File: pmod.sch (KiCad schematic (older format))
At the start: 13 parts, among them J6 PMOD, U10 AP7381-33SA, U11 TXS0108EPW

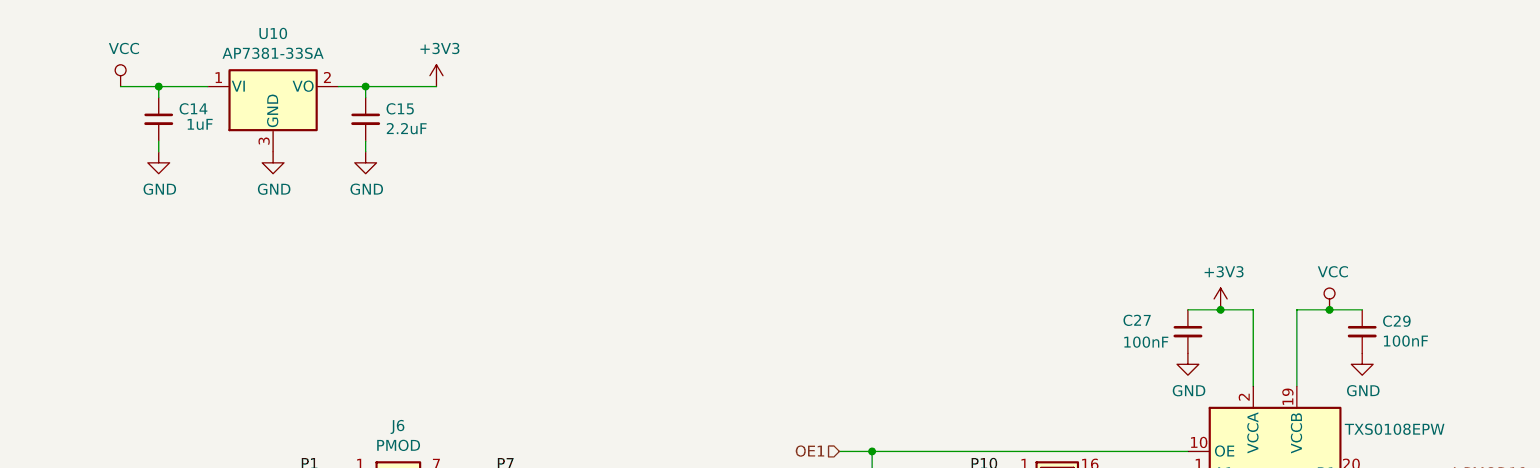
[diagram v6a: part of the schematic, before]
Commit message: replaced VCC with 5V, fixed ROM footprint
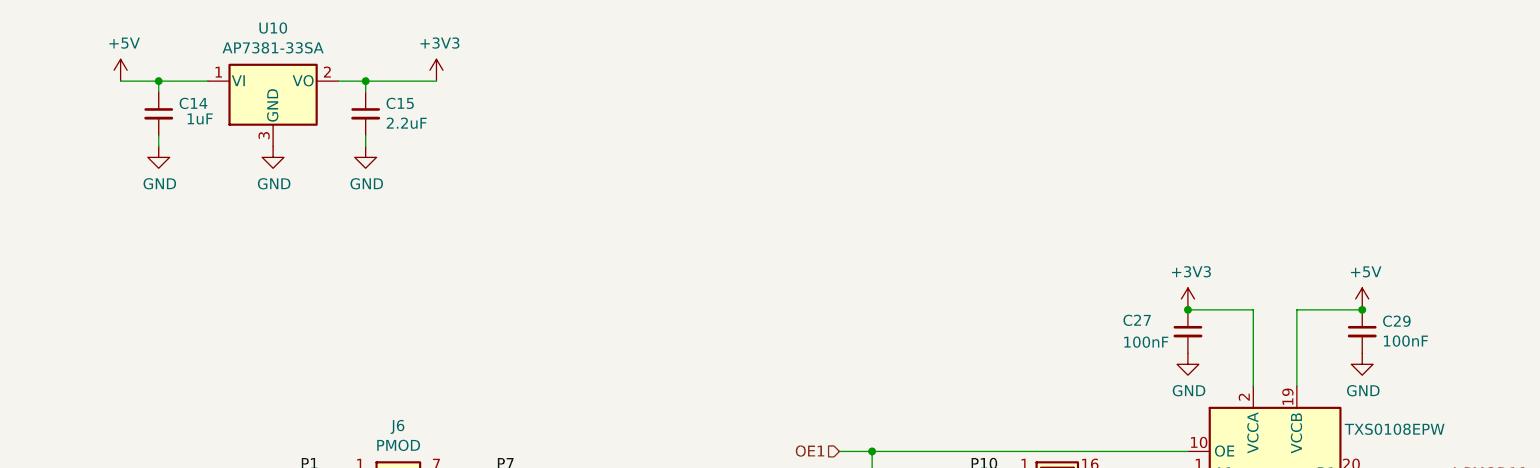
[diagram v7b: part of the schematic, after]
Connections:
- net labels added: +5V
- net labels removed: VCC
- wire segments 68 -> 66
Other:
- moved on the sheet: C14, C15, U10
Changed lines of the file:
@@
 	1925 3800 1925 3400
-$Comp
-L power:VCC #PWR?
-U 1 1 5DC93B40
-P 1850 1625
-AR Path="/5D70CA34/5DC93B40" Ref="#PWR?"  Part="1"
-AR Path="/5D70CA34/5DC790D1/5DC93B40" Ref="#PWR033"  Part="1"
-F 0 "#PWR033" H 1850 1475 50  0001 C CNN
-F 1 "VCC" H 1867 1798 50  0000 C CNN
-F 2 "" H 1850 1625 50  0001 C CNN
-F 3 "" H 1850 1625 50  0001 C CNN
-	1    1850 1625
-	1    0    0    -1
-$EndComp
 $Comp
 L power:+3V3 #PWR?
 U 1 1 5DC93B46
-P 3300 1625
+P 3300 1600
 AR Path="/5D70CA34/5DC93B46" Ref="#PWR?"  Part="1"
 AR Path="/5D70CA34/5DC790D1/5DC93B46" Ref="#PWR077"  Part="1"
-F 0 "#PWR077" H 3300 1475 50  0001 C CNN
-F 1 "+3V3" H 3315 1798 50  0000 C CNN
-F 2 "" H 3300 1625 50  0001 C CNN
-F 3 "" H 3300 1625 50  0001 C CNN
-	1    3300 1625
-	1    0    0    -1
-$EndComp
-Wire Wire Line
-	2025 1625 1850 1625
-Connection ~ 2025 1625
-Wire Wire Line
-	2025 1675 2025 1625
-Wire Wire Line
-	2975 1625 3300 1625
-Connection ~ 2975 1625
-Wire Wire Line
-	2975 1675 2975 1625
-Wire Wire Line
-	2850 1625 2975 1625
-Wire Wire Line
-	2250 1625 2025 1625
+F 0 "#PWR077" H 3300 1450 50  0001 C CNN
+F 1 "+3V3" H 3315 1773 50  0000 C CNN
+F 2 "" H 3300 1600 50  0001 C CNN
+F 3 "" H 3300 1600 50  0001 C CNN
+	1    3300 1600
+	1    0    0    -1
+$EndComp
+Wire Wire Line
+	2025 1600 1850 1600
+Connection ~ 2025 1600
+Wire Wire Line
+	2025 1650 2025 1600
+Wire Wire Line
+	2975 1600 3300 1600
+Connection ~ 2975 1600
+Wire Wire Line
+	2975 1650 2975 1600
+Wire Wire Line
+	2850 1600 2975 1600
+Wire Wire Line
+	2250 1600 2025 1600
 $Comp
 L power:GND #PWR?
 U 1 1 5DC93B54
-P 2550 1925
+P 2550 1900
 AR Path="/5D70CA34/5DC93B54" Ref="#PWR?"  Part="1"
 AR Path="/5D70CA34/5DC790D1/5DC93B54" Ref="#PWR036"  Part="1"
-F 0 "#PWR036" H 2550 1675 50  0001 C CNN
-F 1 "GND" H 2555 1752 50  0000 C CNN
-F 2 "" H 2550 1925 50  0001 C CNN
-F 3 "" H 2550 1925 50  0001 C CNN
-	1    2550 1925
+F 0 "#PWR036" H 2550 1650 50  0001 C CNN
+F 1 "GND" H 2555 1727 50  0000 C CNN
+F 2 "" H 2550 1900 50  0001 C CNN
+F 3 "" H 2550 1900 50  0001 C CNN
+	1    2550 1900
 	1    0    0    -1
 $EndComp
@@
 L power:GND #PWR?
 U 1 1 5DC93B5A
-P 2025 1925
+P 2025 1900
 AR Path="/5D70CA34/5DC93B5A" Ref="#PWR?"  Part="1"
 AR Path="/5D70CA34/5DC790D1/5DC93B5A" Ref="#PWR034"  Part="1"
-F 0 "#PWR034" H 2025 1675 50  0001 C CNN
-F 1 "GND" H 2030 1752 50  0000 C CNN
-F 2 "" H 2025 1925 50  0001 C CNN
-F 3 "" H 2025 1925 50  0001 C CNN
-	1    2025 1925
-	1    0    0    -1
-$EndComp
-Wire Wire Line
-	2025 1875 2025 1925
+F 0 "#PWR034" H 2025 1650 50  0001 C CNN
+F 1 "GND" H 2030 1727 50  0000 C CNN
+F 2 "" H 2025 1900 50  0001 C CNN
+F 3 "" H 2025 1900 50  0001 C CNN
+	1    2025 1900
+	1    0    0    -1
+$EndComp
+Wire Wire Line
+	2025 1850 2025 1900
 $Comp
 L Device:C_Small C?
 U 1 1 5DC93B61
-P 2025 1775
+P 2025 1750
 AR Path="/5D70CA34/5DC93B61" Ref="C?"  Part="1"
 AR Path="/5D70CA34/5DC790D1/5DC93B61" Ref="C14"  Part="1"
-F 0 "C14" H 2117 1821 50  0000 L CNN
-F 1 "1uF" H 2150 1750 50  0000 L CNN
-F 2 "Capacitor_SMD:C_0603_1608Metric_Pad1.05x0.95mm_HandSolder" H 2025 1775 50  0001 C CNN
-F 3 "~" H 2025 1775 50  0001 C CNN
-	1    2025 1775
+F 0 "C14" H 2117 1796 50  0000 L CNN
+F 1 "1uF" H 2150 1725 50  0000 L CNN
+F 2 "Capacitor_SMD:C_0603_1608Metric_Pad1.05x0.95mm_HandSolder" H 2025 1750 50  0001 C CNN
+F 3 "~" H 2025 1750 50  0001 C CNN
+	1    2025 1750
 	1    0    0    -1
 $EndComp
@@
 L power:GND #PWR?
 U 1 1 5DC93B67
-P 2975 1925
+P 2975 1900
 AR Path="/5D70CA34/5DC93B67" Ref="#PWR?"  Part="1"
 AR Path="/5D70CA34/5DC790D1/5DC93B67" Ref="#PWR038"  Part="1"
-F 0 "#PWR038" H 2975 1675 50  0001 C CNN
-F 1 "GND" H 2980 1752 50  0000 C CNN
-F 2 "" H 2975 1925 50  0001 C CNN
-F 3 "" H 2975 1925 50  0001 C CNN
-	1    2975 1925
-	1    0    0    -1
-$EndComp
-Wire Wire Line
-	2975 1875 2975 1925
+F 0 "#PWR038" H 2975 1650 50  0001 C CNN
+F 1 "GND" H 2980 1727 50  0000 C CNN
+F 2 "" H 2975 1900 50  0001 C CNN
+F 3 "" H 2975 1900 50  0001 C CNN
+	1    2975 1900
+	1    0    0    -1
+$EndComp
+Wire Wire Line
+	2975 1850 2975 1900
 $Comp
 L Device:C_Small C?
 U 1 1 5DC93B6E
-P 2975 1775
+P 2975 1750
 AR Path="/5D70CA34/5DC93B6E" Ref="C?"  Part="1"
 AR Path="/5D70CA34/5DC790D1/5DC93B6E" Ref="C15"  Part="1"
-F 0 "C15" H 3067 1821 50  0000 L CNN
-F 1 "2.2uF" H 3067 1730 50  0000 L CNN
-F 2 "Capacitor_SMD:C_0603_1608Metric_Pad1.05x0.95mm_HandSolder" H 2975 1775 50  0001 C CNN
-F 3 "~" H 2975 1775 50  0001 C CNN
-	1    2975 1775
+F 0 "C15" H 3067 1796 50  0000 L CNN
+F 1 "2.2uF" H 3067 1705 50  0000 L CNN
+F 2 "Capacitor_SMD:C_0603_1608Metric_Pad1.05x0.95mm_HandSolder" H 2975 1750 50  0001 C CNN
+F 3 "~" H 2975 1750 50  0001 C CNN
+	1    2975 1750
 	1    0    0    -1
 $EndComp
@@
 L THS-80-rescue:AP7381-33SA-Regulator_Linear U?
 U 1 1 5DC93B74
-P 2550 1625
+P 2550 1600
 AR Path="/5D70CA34/5DC93B74" Ref="U?"  Part="1"
 AR Path="/5D70CA34/5DC790D1/5DC93B74" Ref="U10"  Part="1"
 AR Path="/5DC93B74" Ref="U10"  Part="1"
-F 0 "U10" H 2550 1867 50  0000 C CNN
-F 1 "AP7381-33SA" H 2550 1776 50  0000 C CNN
-F 2 "Package_TO_SOT_SMD:SOT-23" H 2550 1850 50  0001 C CIN
-F 3 "https://www.mouser.com/datasheet/2/115/AP7381-1220674.pdf" H 2550 1575 50  0001 C CNN
-	1    2550 1625
+F 0 "U10" H 2550 1842 50  0000 C CNN
+F 1 "AP7381-33SA" H 2550 1751 50  0000 C CNN
+F 2 "Package_TO_SOT_SMD:SOT-23" H 2550 1825 50  0001 C CIN
+F 3 "https://www.mouser.com/datasheet/2/115/AP7381-1220674.pdf" H 2550 1550 50  0001 C CNN
+	1    2550 1600
 	1    0    0    -1
 $EndComp
@@
 $EndComp
 $Comp
-L power:VCC #PWR?
-U 1 1 5DEF913A
-P 7400 2650
-AR Path="/5D70CA34/5DEF913A" Ref="#PWR?"  Part="1"
-AR Path="/5D70CA34/5DC790D1/5DEF913A" Ref="#PWR0103"  Part="1"
-F 0 "#PWR0103" H 7400 2500 50  0001 C CNN
-F 1 "VCC" H 7417 2823 50  0000 C CNN
-F 2 "" H 7400 2650 50  0001 C CNN
-F 3 "" H 7400 2650 50  0001 C CNN
-	1    7400 2650
-	1    0    0    -1
-$EndComp
-$Comp
 L Logic_LevelTranslator:TXS0108EPW U11
 U 1 1 5DF4B0EE
@@
 L power:+3V3 #PWR0105
 U 1 1 5DF9A54A
-P 6900 2650
-F 0 "#PWR0105" H 6900 2500 50  0001 C CNN
-F 1 "+3V3" H 6915 2823 50  0000 C CNN
-F 2 "" H 6900 2650 50  0001 C CNN
-F 3 "" H 6900 2650 50  0001 C CNN
-	1    6900 2650
+P 6750 2650
+F 0 "#PWR0105" H 6750 2500 50  0001 C CNN
+F 1 "+3V3" H 6765 2823 50  0000 C CNN
+F 2 "" H 6750 2650 50  0001 C CNN
+F 3 "" H 6750 2650 50  0001 C CNN
+	1    6750 2650
 	1    0    0    -1
 $EndComp
@@
 	7250 3000 7250 2650
 Wire Wire Line
-	7250 2650 7400 2650
-Connection ~ 7400 2650
-Wire Wire Line
-	7400 2650 7550 2650
-Wire Wire Line
 	7050 3000 7050 2650
-Wire Wire Line
-	7050 2650 6900 2650
-Connection ~ 6900 2650
-Wire Wire Line
-	6900 2650 6750 2650
+$Comp
+L power:+5V #PWR0128
+U 1 1 5EB06066
+P 1850 1600
+F 0 "#PWR0128" H 1850 1450 50  0001 C CNN
+F 1 "+5V" H 1865 1773 50  0000 C CNN
+F 2 "" H 1850 1600 50  0001 C CNN
+F 3 "" H 1850 1600 50  0001 C CNN
+	1    1850 1600
+	1    0    0    -1
+$EndComp
+Wire Wire Line
+	7250 2650 7550 2650
+$Comp
+L power:+5V #PWR0129
+U 1 1 5EB0BA2B
+P 7550 2650
+F 0 "#PWR0129" H 7550 2500 50  0001 C CNN
+F 1 "+5V" H 7565 2823 50  0000 C CNN
+F 2 "" H 7550 2650 50  0001 C CNN
+F 3 "" H 7550 2650 50  0001 C CNN
+	1    7550 2650
+	1    0    0    -1
+$EndComp
+Connection ~ 7550 2650
+Connection ~ 6750 2650
+Wire Wire Line
+	6750 2650 7050 2650
 $EndSCHEMATC

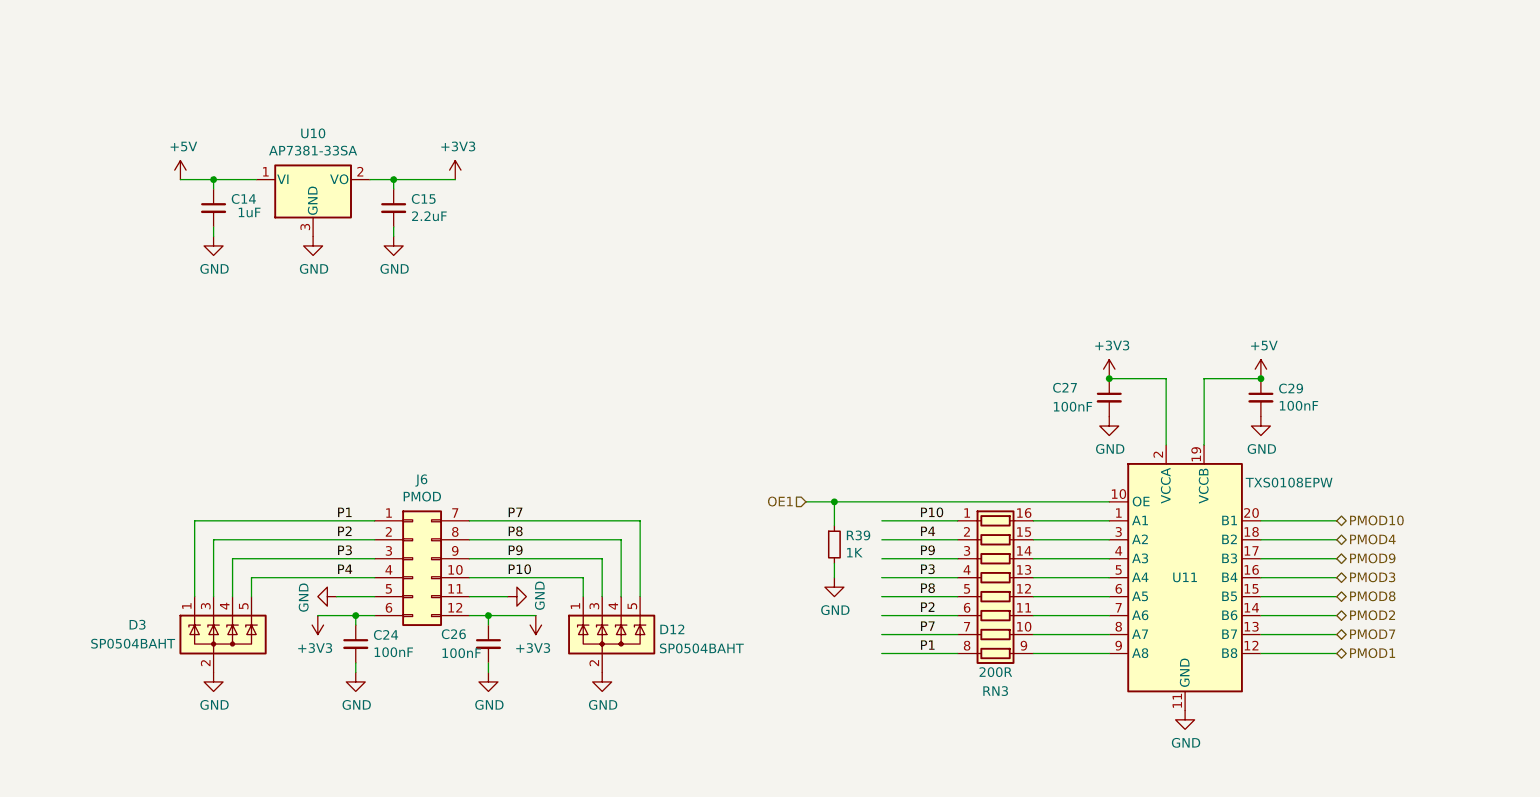
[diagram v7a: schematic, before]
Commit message: layout changes, silkscreen fixes
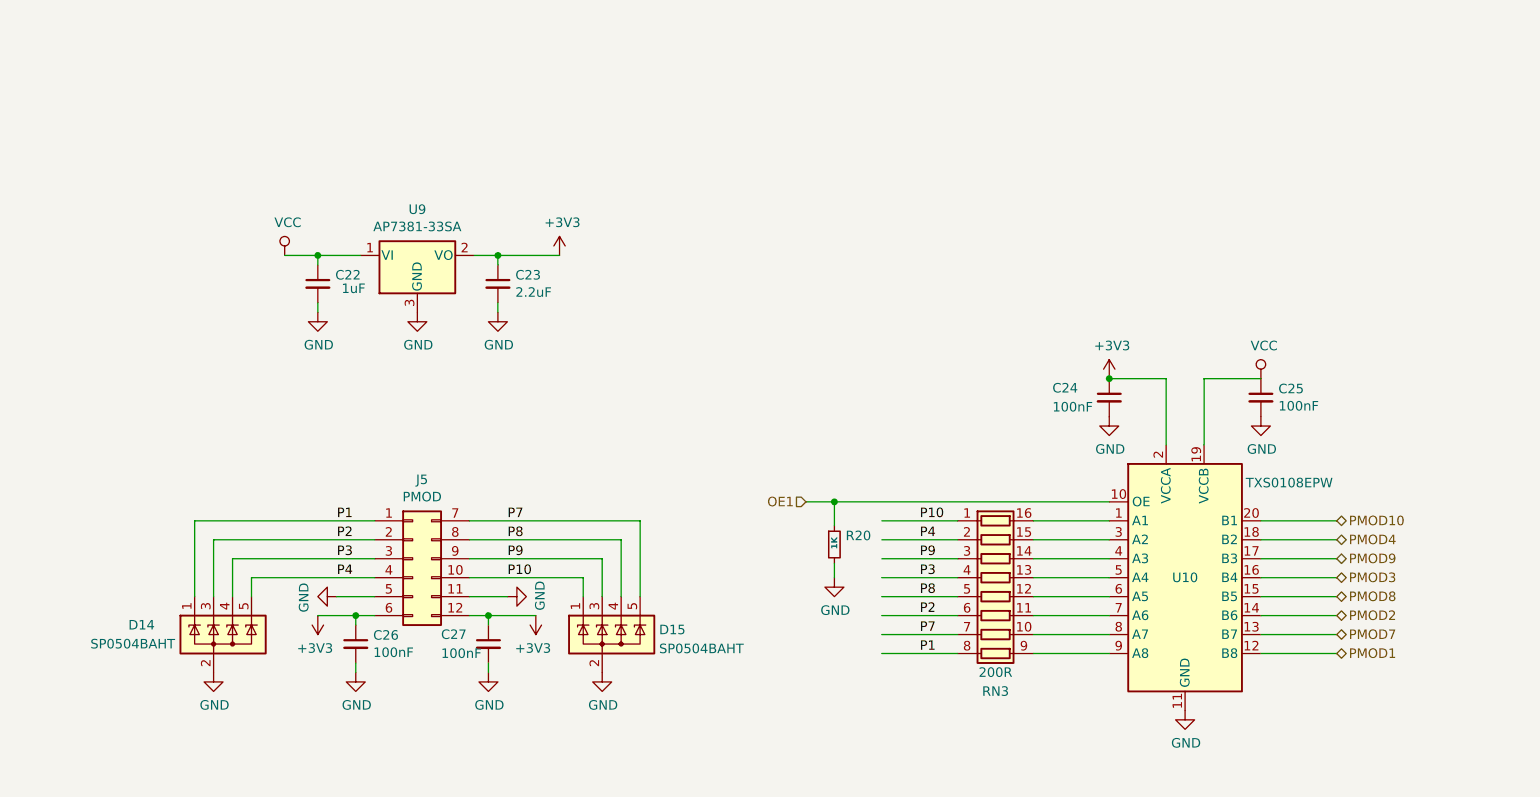
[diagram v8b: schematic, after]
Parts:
- renumbered C14 to C22, C15 to C23, C27 to C24, C29 to C25, C24 to C26, C26 to C27, D3 to D14, D12 to D15, J6 to J5, R39 to R20, U11 to U10, U10 to U9
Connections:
- net labels added: VCC
- net labels removed: +5V
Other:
- moved on the sheet: C22, C23, U9
